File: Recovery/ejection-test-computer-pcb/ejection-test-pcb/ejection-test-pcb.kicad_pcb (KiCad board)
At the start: 2 copper layers, 65.4 x 90.7 mm, 21 parts, among them J1 BATTERY_TERMINAL, J2 LOAD_CELL_CONNECTOR, J3 NICHROME-TERMINAL, Q1 IRLZ34N, SW1 ON, U1 HX7111, U2 LM2596, U3 ESP32_DEVKIT

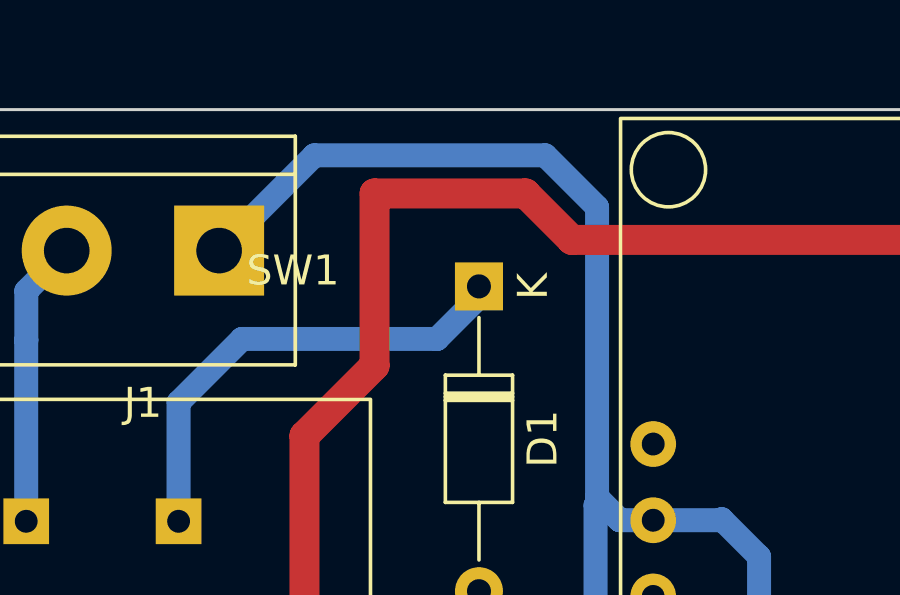
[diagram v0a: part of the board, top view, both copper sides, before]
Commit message: added piston test system flowchart
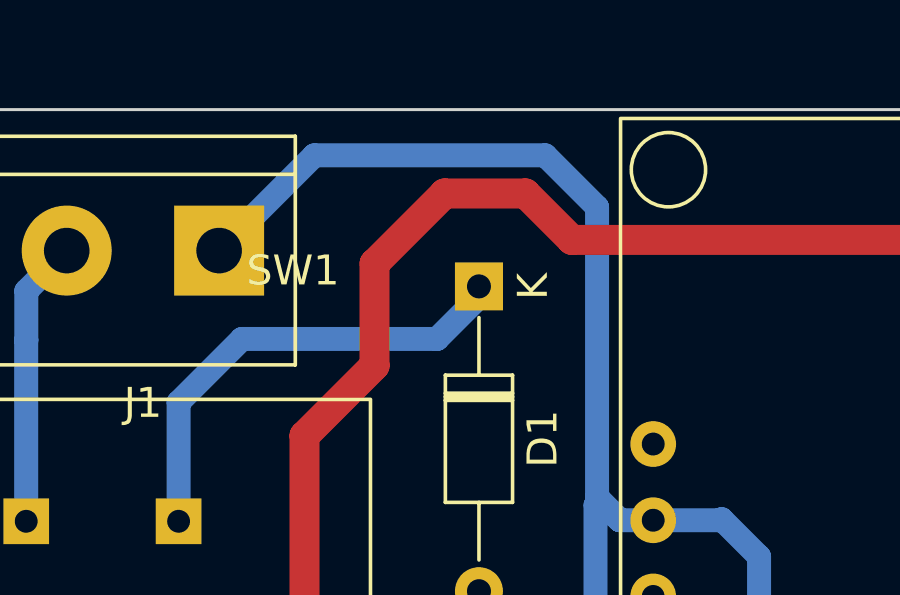
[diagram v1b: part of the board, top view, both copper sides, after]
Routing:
- net 5V: track 195.0 -> 193.7 mm
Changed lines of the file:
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@@
     )
     (pad_to_mask_clearance 0)
+    (grid_origin 238.3028 103.6828)
     (pcbplotparams
       (layerselection 0x0001000_7fffffff)
@@
     (format (units 3) (units_format 1) (precision 4))
     (style (thickness 0.2) (arrow_length 1.27) (text_position_mode 0) (extension_height 0.58642) (extension_offset 0.5) keep_text_aligned)
+  )
+  (dimension (type aligned) (layer "Edge.Cuts")
+    (pts (xy 117.2464 132.3848) (xy 170.942 132.3848))
+    (height 24.9936)
+    (gr_text "53.6956 mm" (at 144.0942 156.2284) (layer "Edge.Cuts")
+      (effects (font (size 1 1) (thickness 0.15)))
+    )
+    (format (units 3) (units_format 1) (precision 4))
+    (style (thickness 0.1) (arrow_length 1.27) (text_position_mode 0) (extension_height 0.58642) (extension_offset 0.5) keep_text_aligned)
+  )
+  (dimension (type aligned) (layer "Edge.Cuts")
+    (pts (xy 110.9726 51.1556) (xy 176.149 51.1556))
+    (height -2.0828)
+    (gr_text "65.1764 mm" (at 143.5608 47.9228) (layer "Edge.Cuts")
+      (effects (font (size 1 1) (thickness 0.15)))
+    )
+    (format (units 3) (units_format 1) (precision 4))
+    (style (thickness 0.1) (arrow_length 1.27) (text_position_mode 0) (extension_height 0.58642) (extension_offset 0.5) keep_text_aligned)
+  )
+  (dimension (type aligned) (layer "Edge.Cuts")
+    (pts (xy 117.221 133.604) (xy 110.744 133.604))
+    (height 3.7592)
+    (gr_text "6.4770 mm" (at 113.9825 128.6948) (layer "Edge.Cuts")
+      (effects (font (size 1 1) (thickness 0.15)))
+    )
+    (format (units 3) (units_format 1) (precision 4))
+    (style (thickness 0.1) (arrow_length 1.27) (text_position_mode 0) (extension_height 0.58642) (extension_offset 0.5) keep_text_aligned)
+  )
+  (dimension (type aligned) (layer "Edge.Cuts")
+    (pts (xy 175.387 133.604) (xy 175.387 141.8844))
+    (height -4.6482)
+    (gr_text "8.2804 mm" (at 178.8852 137.7442 90) (layer "Edge.Cuts")
+      (effects (font (size 1 1) (thickness 0.15)))
+    )
+    (format (units 3) (units_format 1) (precision 4))
+    (style (thickness 0.1) (arrow_length 1.27) (text_position_mode 0) (extension_height 0.58642) (extension_offset 0.5) keep_text_aligned)
   )
   (segment (start 160.5788 91.3384) (end 160.5788 59.3344) (width 0.8) (layer "B.Cu") (net 1))
@@
   (segment (start 134.239 135.3058) (end 131.9022 137.6426) (width 0.8) (layer "B.Cu") (net 17))
   (segment (start 119.9464 120.992) (end 133.2094 120.992) (width 0.8) (layer "B.Cu") (net 17))
-  (segment (start 132.588 53.9496) (end 137.6172 53.9496) (width 1) (layer "F.Cu") (net 20))
+  (segment (start 132.588 56.2864) (end 134.9248 53.9496) (width 1) (layer "F.Cu") (net 20))
+  (segment (start 161.9504 55.499) (end 162.5346 56.0832) (width 1) (layer "F.Cu") (net 20))
+  (segment (start 137.6172 53.9496) (end 139.1666 55.499) (width 1) (layer "F.Cu") (net 20))
+  (segment (start 124.7902 76.962) (end 130.2512 71.501) (width 1) (layer "F.Cu") (net 20))
+  (segment (start 134.9248 53.9496) (end 137.6172 53.9496) (width 1) (layer "F.Cu") (net 20))
+  (segment (start 162.5346 56.0832) (end 162.5346 60.2488) (width 1) (layer "F.Cu") (net 20))
+  (segment (start 132.588 59.69) (end 132.588 56.2864) (width 1) (layer "F.Cu") (net 20))
   (segment (start 130.2512 71.501) (end 130.2512 62.0268) (width 1) (layer "F.Cu") (net 20))
   (segment (start 139.1666 55.499) (end 161.9504 55.499) (width 1) (layer "F.Cu") (net 20))
-  (segment (start 132.588 59.69) (end 132.588 53.9496) (width 1) (layer "F.Cu") (net 20))
   (segment (start 130.2512 62.0268) (end 132.588 59.69) (width 1) (layer "F.Cu") (net 20))
-  (segment (start 124.7902 76.962) (end 130.2512 71.501) (width 1) (layer "F.Cu") (net 20))
-  (segment (start 162.5346 56.0832) (end 162.5346 60.2488) (width 1) (layer "F.Cu") (net 20))
-  (segment (start 161.9504 55.499) (end 162.5346 56.0832) (width 1) (layer "F.Cu") (net 20))
-  (segment (start 137.6172 53.9496) (end 139.1666 55.499) (width 1) (layer "F.Cu") (net 20))
   (via (at 124.7902 76.962) (size 0.8) (drill 0.4) (layers "F.Cu" "B.Cu") (net 20))
   (via (at 162.5346 60.2488) (size 0.8) (drill 0.4) (layers "F.Cu" "B.Cu") (net 20))

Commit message: added test pcb
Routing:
- net LED3: track 54.3 -> 54.9 mm

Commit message: added paho-mqtt-client for test app
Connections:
- D1 pad 2: 11V -> 11.1V
- U2 pad 1: 11V -> 11.1V
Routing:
- net 11V: track 55.2 -> 0.00 mm
- net 11.1V: track 0.00 -> 55.2 mm

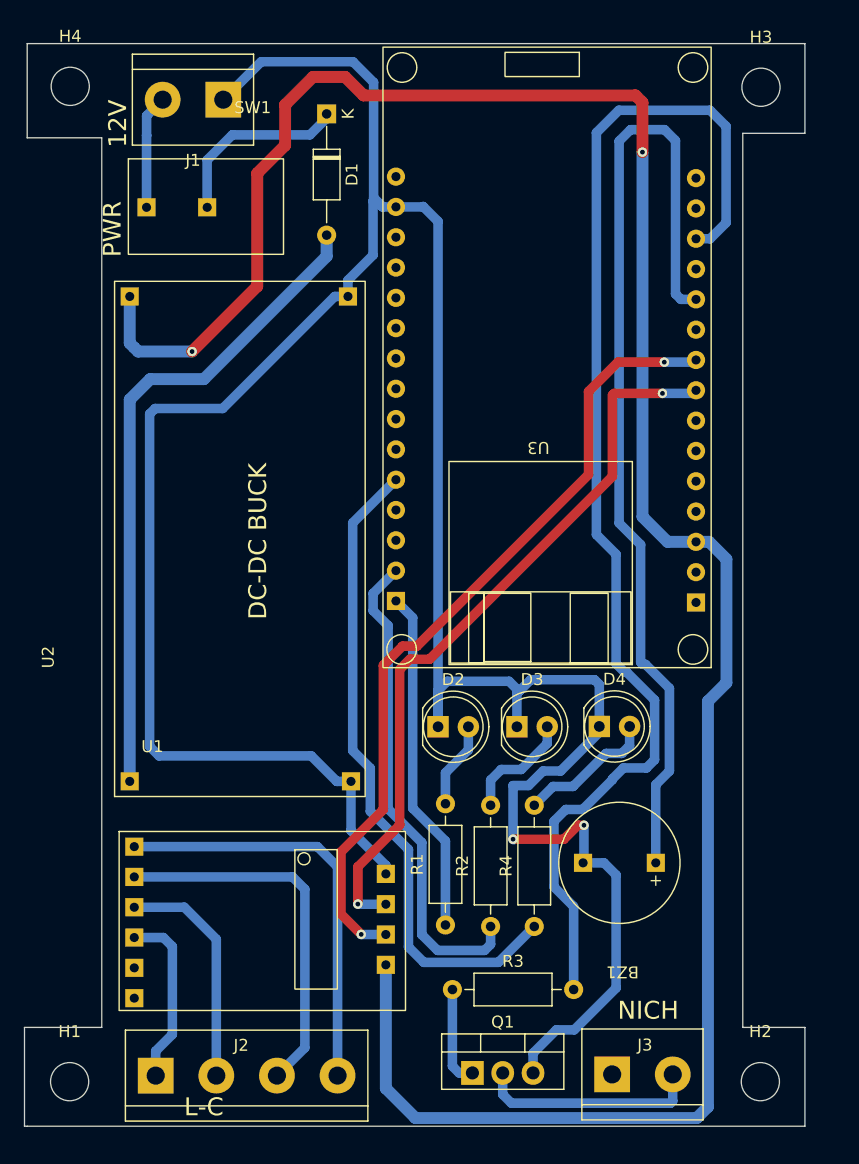
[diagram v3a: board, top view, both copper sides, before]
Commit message: updated nichrome counter time
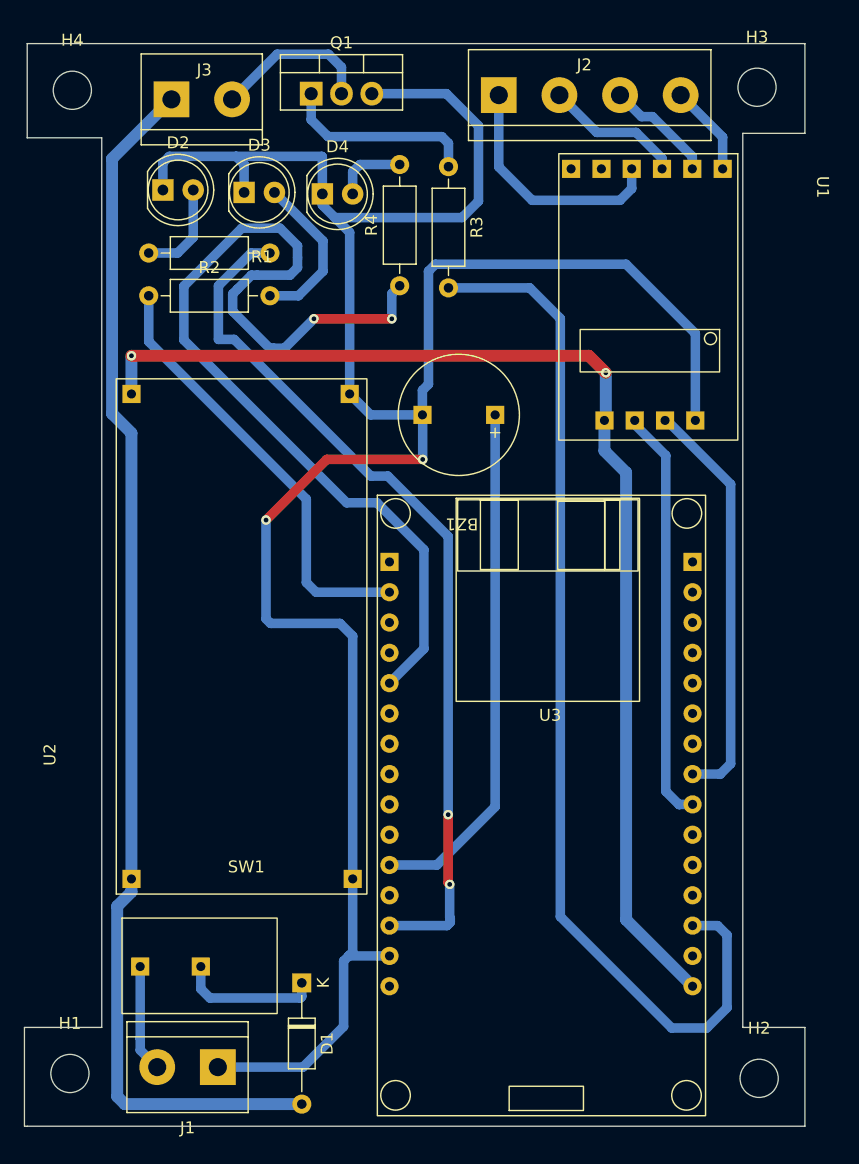
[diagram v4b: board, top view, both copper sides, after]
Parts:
- moved J3 89.7 mm to (123.1, 55.8)
- moved J2 87.1 mm to (150.5, 55.5)
- moved Q1 83.2 mm to (134.8, 55.4)
- moved J1 81.1 mm to (126.9, 136.9)
- moved U1 76.9 mm to (170.5, 60.4), turned to -90 degrees
- moved D1 72.9 mm to (134.0, 129.9)
- moved R3 69.0 mm to (146.3, 61.5), turned to -90 degrees
- moved SW1 63.6 mm to (118.9, 124.4)
- moved R2 60.1 mm to (121.2, 72.3), turned to 0 degrees
- moved R1 58.2 mm to (131.3, 68.7), turned to 180 degrees
- moved R4 54.9 mm to (142.2, 71.5)
- moved D2 50.5 mm to (122.3, 63.4)
- moved D4 50.3 mm to (135.7, 63.8)
- moved D3 50.3 mm to (129.2, 63.6)
- moved BZ1 39.9 mm to (147.1, 82.3)
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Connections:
- U3 pad 11: BUZZER -> unconnected-(U3-Pad11)
- U3 pad 15: unconnected-(U3-Pad15) -> 5V
- U3 pad 18: unconnected-(U3-Pad18) -> LED1
- U3 pad 20: unconnected-(U3-Pad20) -> BUZZER
- U3 pad 3: 5V -> unconnected-(U3-Pad3)
- U3 pad 30: LED1 -> unconnected-(U3-Pad30)
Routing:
- net 5V: track 193.7 -> 98.1 mm
- net 11.1V: track 55.2 -> 102.5 mm
- net LED1: track 28.9 -> 73.7 mm, vias 0 -> 2
- net BUZZER: track 83.1 -> 43.7 mm
- net SCK: track 67.7 -> 34.9 mm, vias 2 -> 0
- net LED3: track 54.9 -> 84.7 mm, vias 0 -> 2
- net Net-(J2-Pad4): track 35.2 -> 7.64 mm
- net DT: track 62.0 -> 34.7 mm, vias 2 -> 0
- net GND: track 230.2 -> 203.9 mm
- net Net-(J2-Pad3): track 31.3 -> 9.23 mm
- net NICHROME_PULSE: track 103.4 -> 88.4 mm
- net Net-(Q1-Pad1): track 8.34 -> 16.5 mm
- net Net-(J2-Pad2): track 19.4 -> 11.7 mm
- net Net-(D4-Pad2): track 11.7 -> 6.05 mm
- net Net-(J2-Pad1): track 15.1 -> 20.4 mm
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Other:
- board text removed: "12V"
- board text removed: "DC-DC BUCK"
- board text removed: "L-C"
- board text removed: "NICH"
- board text removed: "PWR"
